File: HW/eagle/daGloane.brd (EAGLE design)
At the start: 100 x 80 mm, 101 parts, among them IC1 MCP1252-33X50, U1 STM32F10XTXU6, X2 SPARKFUN-CONNECTORS_USB-MICROB

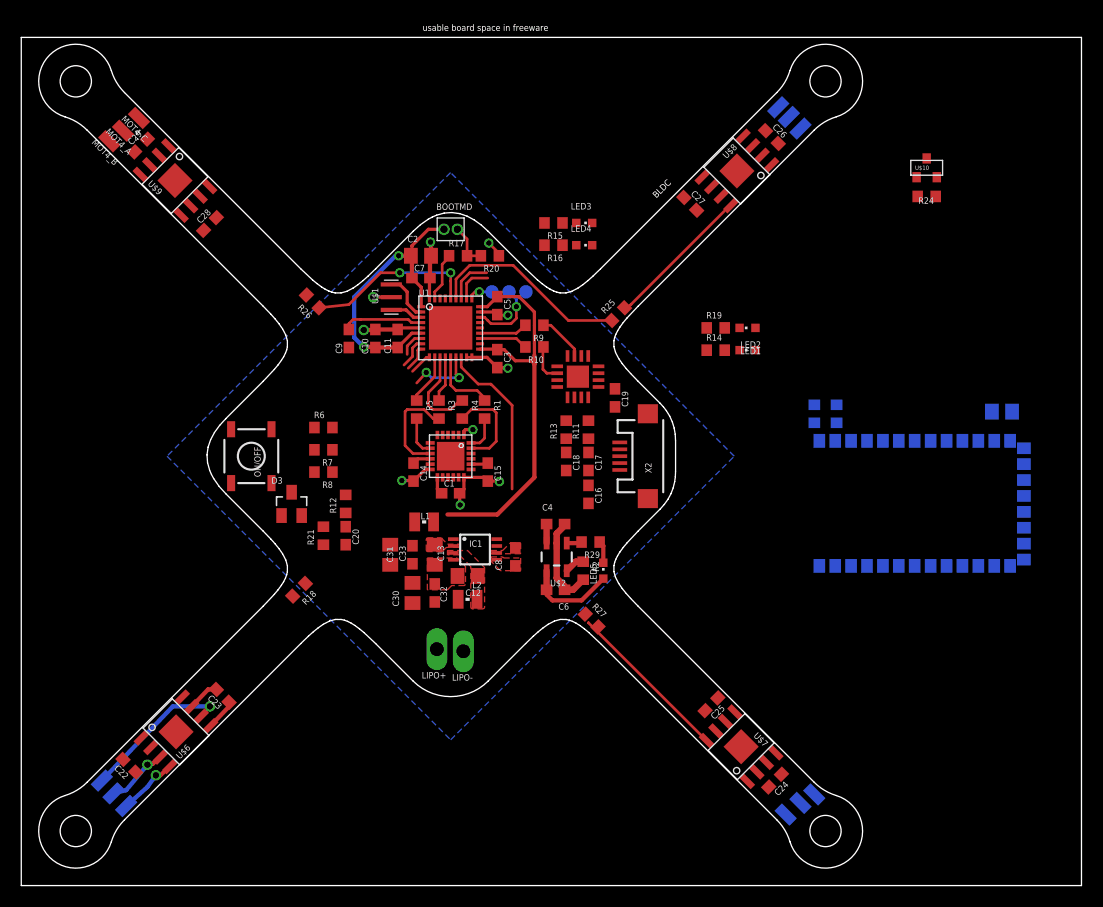
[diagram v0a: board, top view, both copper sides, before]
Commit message: motor driver layout
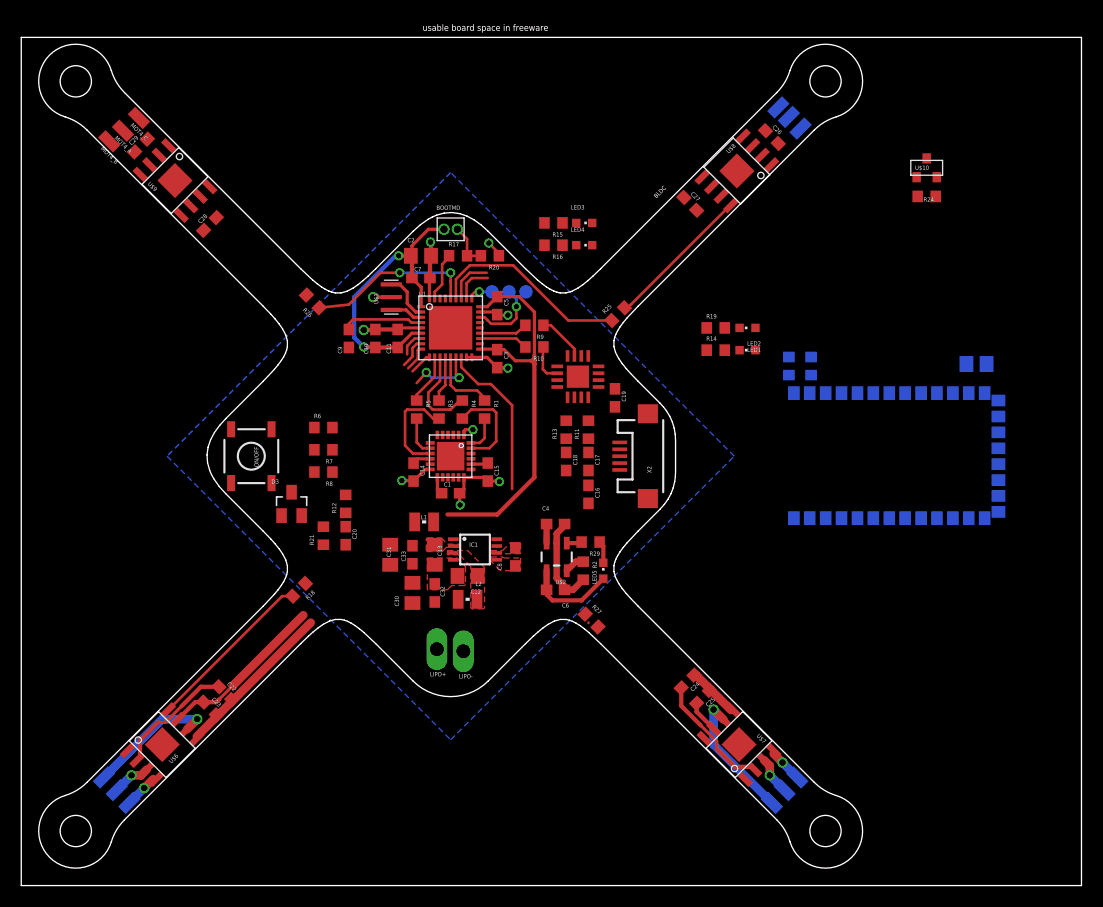
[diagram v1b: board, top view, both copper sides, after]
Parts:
- moved C24 12.5 mm to (62.9, 19.2)
- moved C22 11.4 mm to (19.2, 18.1)
- moved C21 5.10 mm to (90.1, 49.2)
- moved R23 5.10 mm to (74.5, 49.0)
- moved R22 5.10 mm to (72.4, 49.0)
- moved U$5 5.10 mm to (77.2, 40.7)
- moved MOT2_C 4.08 mm to (70.8, 7.80)
- moved MOT2_B 2.42 mm to (73.2, 10.2)
- moved MOT2_A 2.30 mm to (72.0, 9.00)
- moved U$6 1.77 mm to (13.3, 13.3)
- moved C23 1.70 mm to (17.8, 16.7)
- moved C25 1.06 mm to (64.3, 17.8)
- moved MOT1_A 0.42 mm to (9.00, 9.00)
- moved MOT1_B 0.42 mm to (10.2, 7.80)
- moved MOT1_C 0.36 mm to (7.80, 10.2)
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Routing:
- net MOT_GND: track 2.91 -> 20.9 mm
- net N$22: track 0.00 -> 16.2 mm
- net LIPO: track 4.84 -> 20.8 mm
- net N$39: track 15.8 -> 0.02 mm
- net N$31: track 0.00 -> 12.4 mm, vias 0 -> 1
- net N$26: track 0.00 -> 11.5 mm
- net N$32: track 0.00 -> 11.5 mm
- net MOT1_A1: track 0.00 -> 3.64 mm, vias 0 -> 1
- net N$30: track 0.00 -> 3.47 mm, vias 0 -> 1
- net N$27: track 5.72 -> 3.47 mm
- net MOT1_A: track 5.85 -> 3.64 mm
- net N$29: track 14.5 -> 12.4 mm

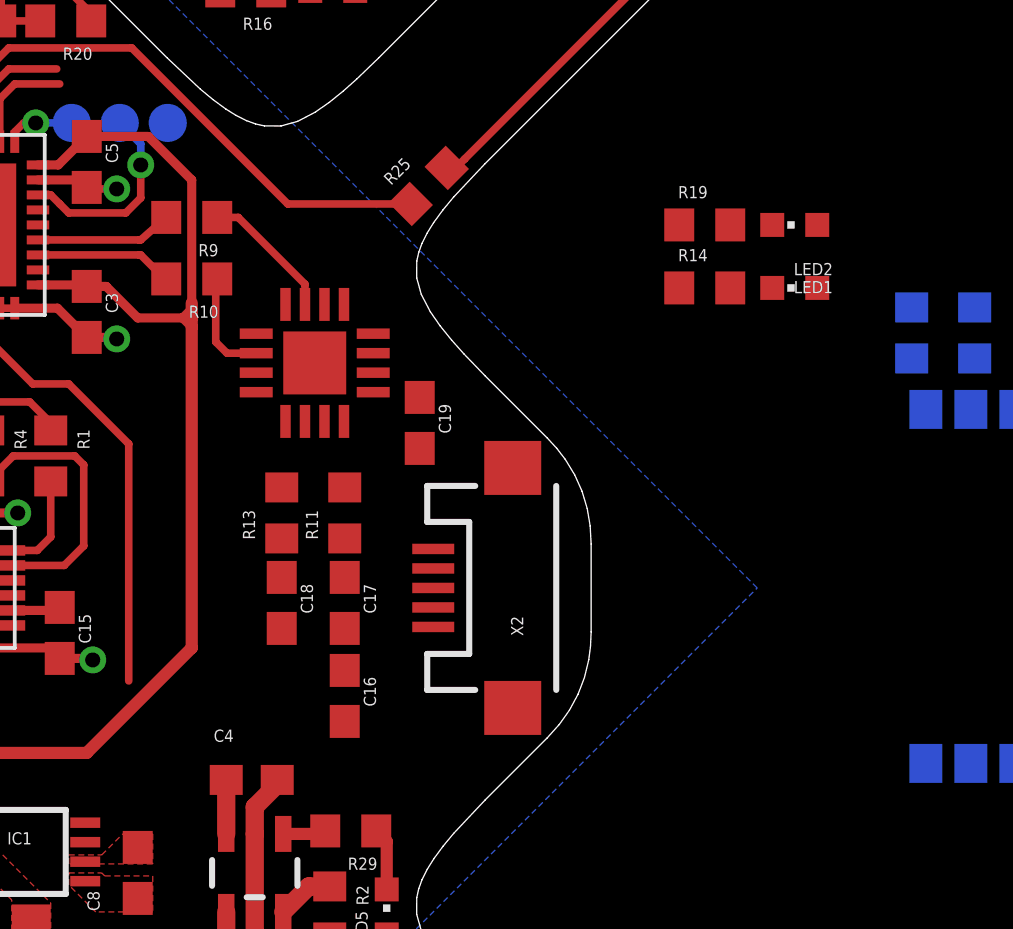
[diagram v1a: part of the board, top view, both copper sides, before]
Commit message: changed layout(usb)
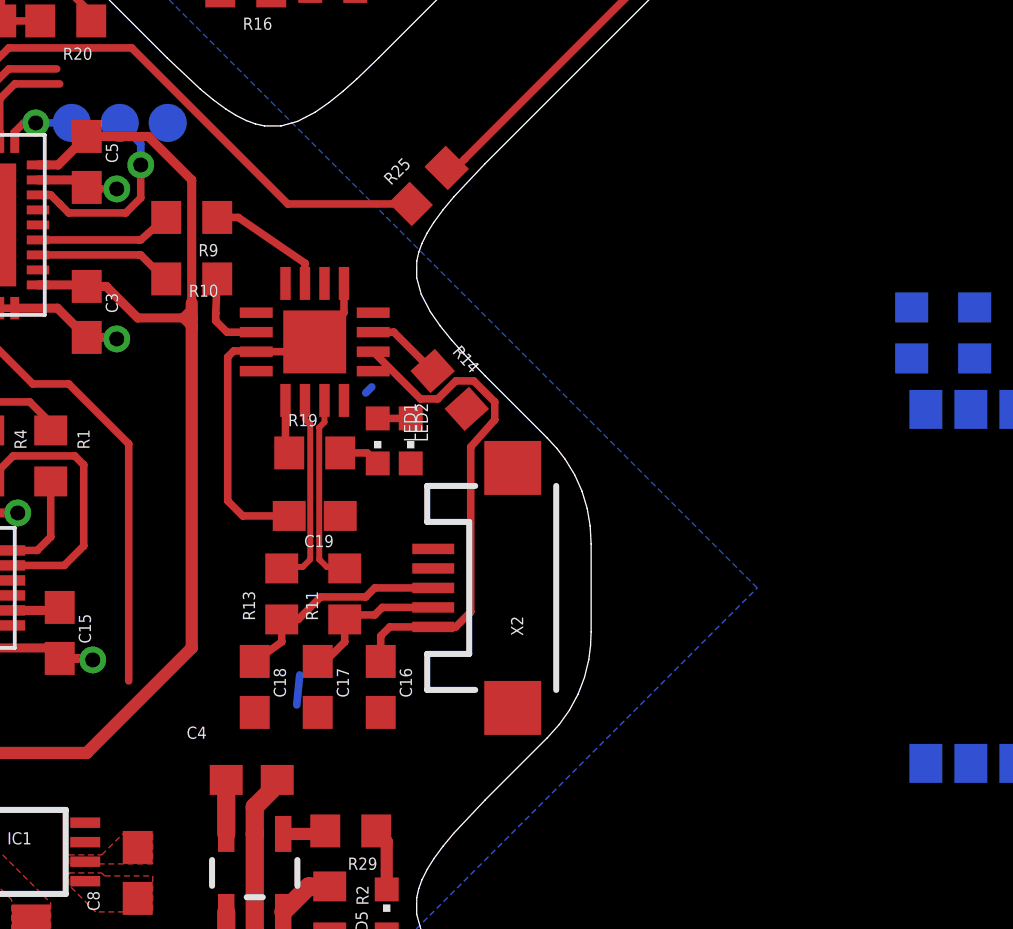
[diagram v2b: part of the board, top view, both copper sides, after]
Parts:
- moved LED2 15.7 mm to (54.6, 45.4), turned to 180 degrees
- moved R19 15.1 mm to (52.5, 45.0)
- moved LED1 13.8 mm to (55.7, 45.4), turned to 180 degrees
- moved R14 9.15 mm to (57.0, 47.1), turned to 312 degrees
- moved C19 4.68 mm to (52.5, 42.9), turned to 180 degrees
- moved C17 2.94 mm to (52.6, 37.2)
- moved C18 2.94 mm to (50.5, 37.2)
- moved R11 2.70 mm to (53.5, 40.3)
- moved R13 2.70 mm to (51.4, 40.3)
- moved C16 1.24 mm to (54.7, 37.2)
- moved U$4 0.70 mm to (52.5, 48.7)
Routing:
- net VBUS: track 8.68 -> 25.4 mm
- net GND: track 42.1 -> 55.7 mm
- net D+: track 0.00 -> 7.35 mm
- net N$17: track 0.00 -> 6.45 mm
- net N$16: track 0.00 -> 6.35 mm
- net D-: track 0.00 -> 5.11 mm
- net N$11: track 0.00 -> 2.52 mm
- net N$12: track 0.00 -> 1.80 mm
- net N$1: track 0.00 -> 1.39 mm
- net VCCIO: track 0.00 -> 1.38 mm
- net N$21: track 3.63 -> 2.91 mm

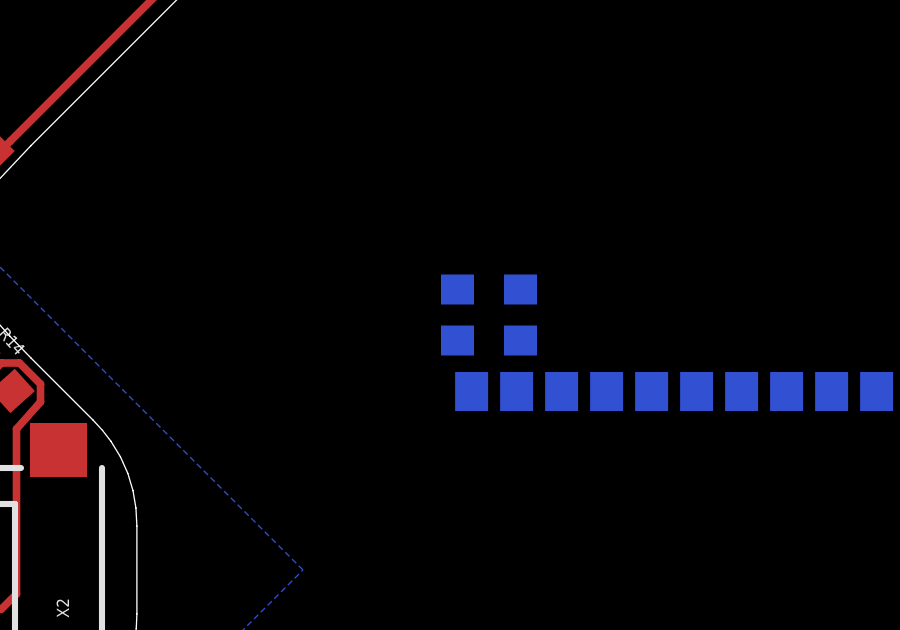
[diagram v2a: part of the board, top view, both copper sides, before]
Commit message: changed layout (usb)
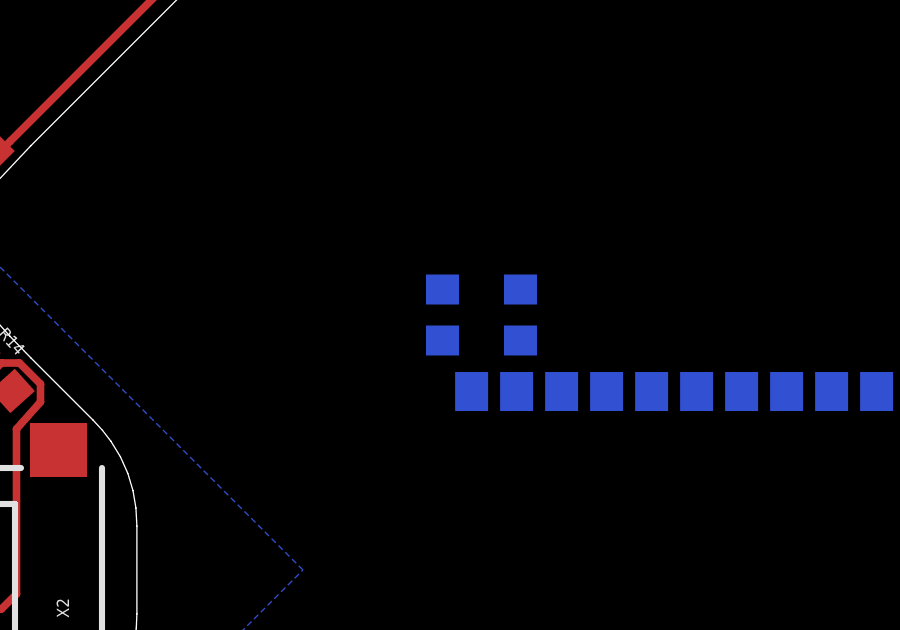
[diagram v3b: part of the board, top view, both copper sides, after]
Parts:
- moved R22 0.50 mm to (71.9, 49.0)
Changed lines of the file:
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@@
 <attribute name="VALUE" x="88.830003125" y="51.74" size="0.4064" layer="28" rot="MR180"/>
 </element>
-<element name="R22" library="rcl" package="R0603" value="1k" x="72.4" y="49" smashed="yes" rot="MR270">
-<attribute name="NAME" x="71.511" y="49.889" size="0.4064" layer="26" rot="MR270"/>
-<attribute name="VALUE" x="74.432003125" y="49.889" size="0.4064" layer="28" rot="MR270"/>
+<element name="R22" library="rcl" package="R0603" value="1k" x="71.9" y="49" smashed="yes" rot="MR270">
+<attribute name="NAME" x="71.011" y="49.889" size="0.4064" layer="26" rot="MR270"/>
+<attribute name="VALUE" x="73.932003125" y="49.889" size="0.4064" layer="28" rot="MR270"/>
 </element>
 <element name="R23" library="rcl" package="R0603" value="1k" x="74.5" y="49" smashed="yes" rot="MR270">
@@
 <wire x1="38.5" y1="49.825" x2="38.225" y2="49.825" width="0.254" layer="1"/>
 <wire x1="38.225" y1="49.825" x2="36.9" y2="48.5" width="0.254" layer="1"/>
-<wire x1="38.5" y1="49.825" x2="72.4" y2="49.85" width="0" layer="19" extent="1-16"/>
+<wire x1="38.5" y1="49.825" x2="71.9" y2="49.85" width="0" layer="19" extent="1-16"/>
 </signal>
 <signal name="USART2_TX">
@@
 <contactref element="U$5" pad="P$1"/>
 <contactref element="R22" pad="2"/>
-<wire x1="72.4" y1="48.15" x2="72.87" y2="46.45" width="0" layer="19" extent="16-16"/>
+<wire x1="71.9" y1="48.15" x2="72.87" y2="46.45" width="0" layer="19" extent="16-16"/>
 </signal>
 <signal name="N$15">

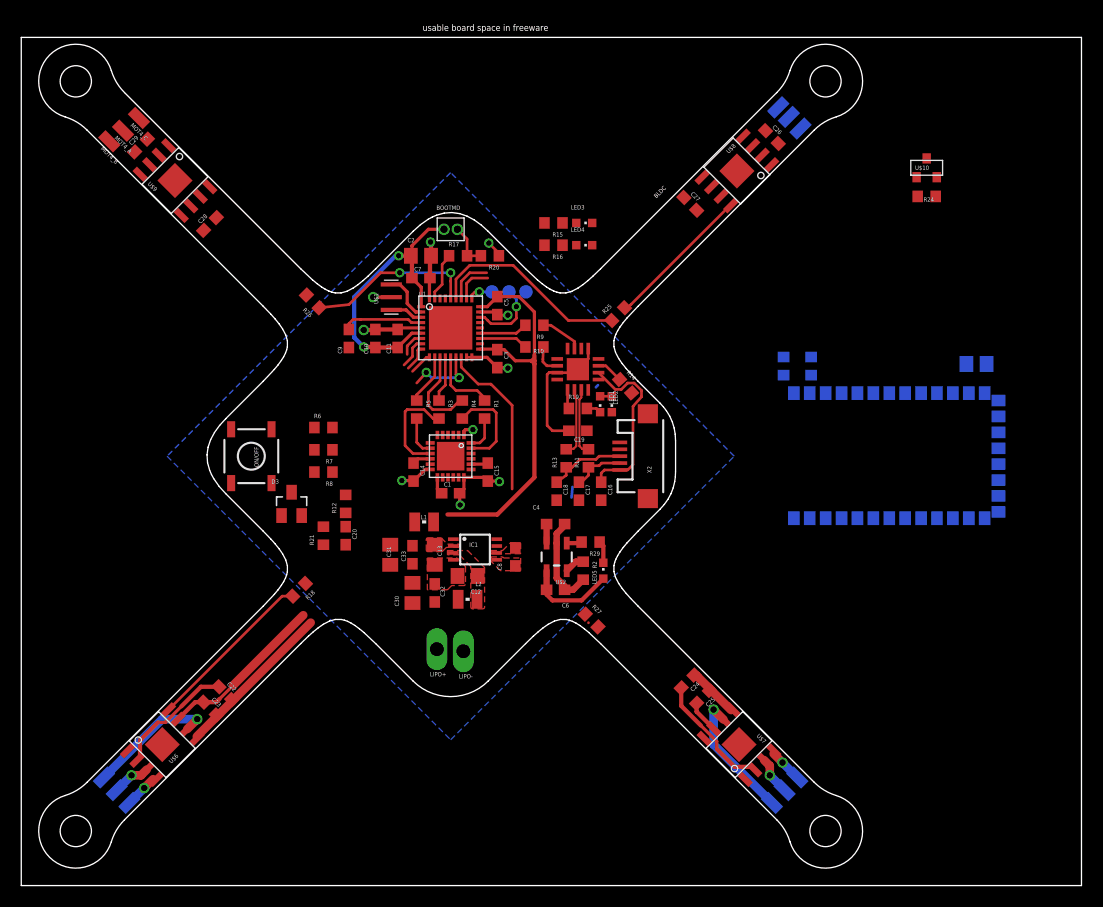
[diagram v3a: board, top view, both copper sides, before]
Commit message: BLDC driver ICs removed dummy symbol for 3A BLDC Controllers added
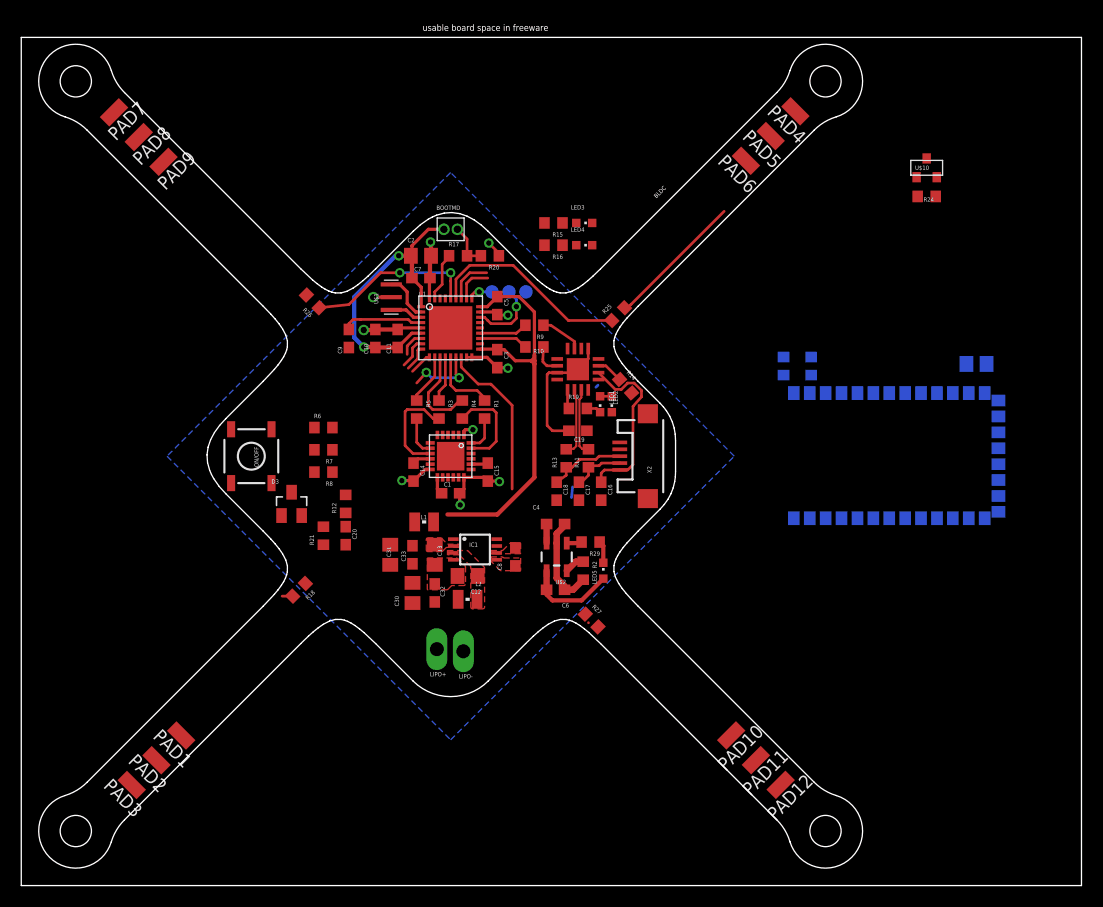
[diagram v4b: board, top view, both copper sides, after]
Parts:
- removed C22, C23, C24, C25, C26, C27, C28, C29: 1µF, rcl:C0603
- removed MOT1_A, MOT1_B, MOT1_C, MOT2_A, MOT2_B, MOT2_C, MOT3_A, MOT3_B, MOT3_C, MOT4_A, MOT4_B, MOT4_C: (no value), daGloane:SMD1,0-2,0
- removed U$6, U$7, U$8, U$9: MTD6501C, daGloane:SOP-8
- added PAD1, PAD10, PAD11, PAD12, PAD2, PAD3, PAD4, PAD5, PAD6, PAD7, PAD8, PAD9: (no value), daGloane:SMD1,27-2,54
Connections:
- removed net MOT1_A: MOT1_A.1, U$6.3
- removed net MOT1_A1: MOT2_A.1, U$7.3
- removed net MOT1_A2: MOT3_A.1, U$8.3
- removed net MOT1_A3: MOT4_A.1, U$9.3
- removed net N$26: C22.2, U$6.2
- removed net N$27: MOT1_B.1, U$6.4
- removed net N$29: MOT1_C.1, U$6.6
- removed net N$30: MOT2_B.1, U$7.4
- removed net N$31: MOT2_C.1, U$7.6
- removed net N$32: C24.2, U$7.2
- removed net N$33: MOT3_B.1, U$8.4
- removed net N$34: MOT3_C.1, U$8.6
- removed net N$35: C26.2, U$8.2
- removed net N$36: MOT4_B.1, U$9.4
- removed net N$37: MOT4_C.1, U$9.6
- removed net N$38: C28.2, U$9.2
- net LIPO: now also PAD1.1, PAD10.1, PAD4.1, PAD7.1; no longer C23.2, C25.2, C27.2, C29.2, U$6.7, U$7.7, U$8.7, U$9.7
- net MOT_GND: now also PAD12.1, PAD3.1, PAD6.1, PAD9.1; no longer C22.1, C23.1, C24.1, C25.1, C26.1, C27.1, C28.1, C29.1, U$6.5, U$7.5, U$8.5, U$9.5
- net N$22: now also PAD2.1; no longer U$6.8
- net N$39: now also PAD11.1; no longer U$7.8
- net N$40: now also PAD5.1; no longer U$8.8
- net N$41: now also PAD8.1; no longer U$9.8
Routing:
- net MOT_GND: track 20.9 -> 0.00 mm
- net LIPO: track 20.8 -> 1.80 mm
- net N$22: track 16.2 -> 0.99 mm
- net N$29: track 12.4 -> 0.00 mm, vias 1 -> 0
- net N$31: track 12.4 -> 0.00 mm, vias 1 -> 0
- net N$26: track 11.5 -> 0.00 mm
- net N$32: track 11.5 -> 0.00 mm
- net MOT1_A1: track 3.64 -> 0.00 mm, vias 1 -> 0
- net MOT1_A: track 3.64 -> 0.00 mm, vias 1 -> 0
- net N$30: track 3.47 -> 0.00 mm, vias 1 -> 0
- net N$27: track 3.47 -> 0.00 mm, vias 1 -> 0
